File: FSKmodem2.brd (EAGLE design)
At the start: 32.1 x 16.5 mm, 9 parts, among them IC1 TCM3105

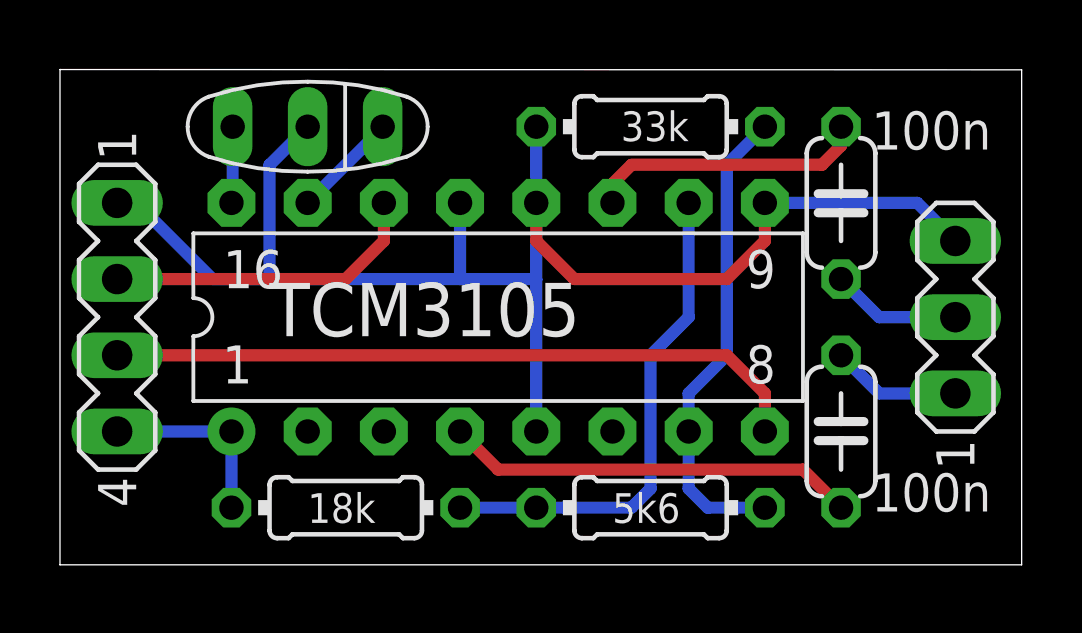
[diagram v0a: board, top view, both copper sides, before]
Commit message: Change to 5mm long resistors
This also makes boards smaller ~ 30x17mm
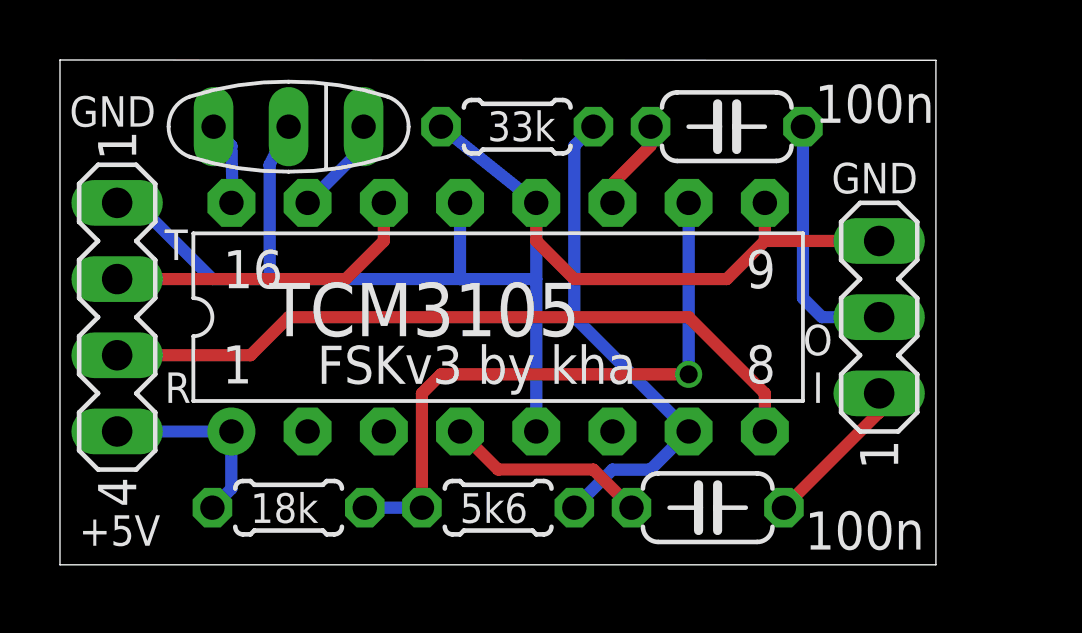
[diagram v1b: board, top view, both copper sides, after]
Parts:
- R1, R2, R3: device rcl:0204/7 -> rcl:0204/5
- moved C1 5.12 mm to (21.6, 1.91), turned to 0 degrees
- moved R2 5.08 mm to (14.6, 1.91)
- moved C2 4.58 mm to (22.2, 14.6), turned to 0 degrees
- moved R3 4.44 mm to (15.2, 14.6)
- moved SV1 2.54 mm to (27.3, 8.26)
- moved R1 1.91 mm to (7.62, 1.91)
- moved Q1 0.64 mm to (7.62, 14.6)
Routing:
- net N$4: track 13.8 -> 6.77 mm
- net N$5: track 9.42 -> 3.07 mm
- net N$3: track 4.34 -> 8.52 mm
- net N$1: track 16.7 -> 20.6 mm, vias 0 -> 1
- net GND: track 51.4 -> 49.5 mm
- net N$9: track 23.4 -> 24.4 mm
- net N$7: track 15.9 -> 16.9 mm
- net N$6: track 4.34 -> 5.13 mm
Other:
- board size 32.1 x 16.5 mm -> 29.2 x 16.8 mm
- board text added: "FSKv3 by kha"
- board text added: "I"
- board text added: "O"
- board text added: "R"
- board text added: "T"
- board text removed: "Ain"
- board text removed: "Aout"
- board text removed: "FSKv2 by kha"
- board text removed: "RXD"
- board text removed: "TXD"

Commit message: round corners a bit
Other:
- outline, holes or cut-outs redrawn
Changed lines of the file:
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@@
 <board>
 <plain>
-<wire x1="0" y1="0" x2="29.1975" y2="0" width="0" layer="20"/>
-<wire x1="29.1975" y1="0" x2="29.1975" y2="16.8175" width="0" layer="20"/>
-<wire x1="29.1975" y1="16.8175" x2="0" y2="16.8275" width="0" layer="20"/>
-<wire x1="0" y1="16.8275" x2="0" y2="0" width="0" layer="20"/>
+<wire x1="0.635" y1="0" x2="28.5625" y2="0" width="0" layer="20"/>
+<wire x1="28.5625" y1="0" x2="29.21" y2="0.635" width="0" layer="20"/>
+<wire x1="29.21" y1="0.635" x2="29.21" y2="16.1925" width="0" layer="20"/>
+<wire x1="29.21" y1="16.1925" x2="28.5625" y2="16.8175" width="0" layer="20"/>
+<wire x1="28.5625" y1="16.8175" x2="0.635" y2="16.8275" width="0" layer="20"/>
+<wire x1="0.635" y1="16.8275" x2="0" y2="16.1925" width="0" layer="20"/>
+<wire x1="0" y1="16.1925" x2="0" y2="0.635" width="0" layer="20"/>
+<wire x1="0" y1="0.635" x2="0.635" y2="0" width="0" layer="20"/>
 <text x="6.985" y="7.62" size="1.778" layer="25">TCM3105</text>
 <text x="25.7175" y="12.3825" size="1.016" layer="25">GND</text>
